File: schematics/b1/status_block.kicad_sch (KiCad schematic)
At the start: 24 parts, among them Q1 2N3904, SW9 SW_SPDT, U3 74HC595

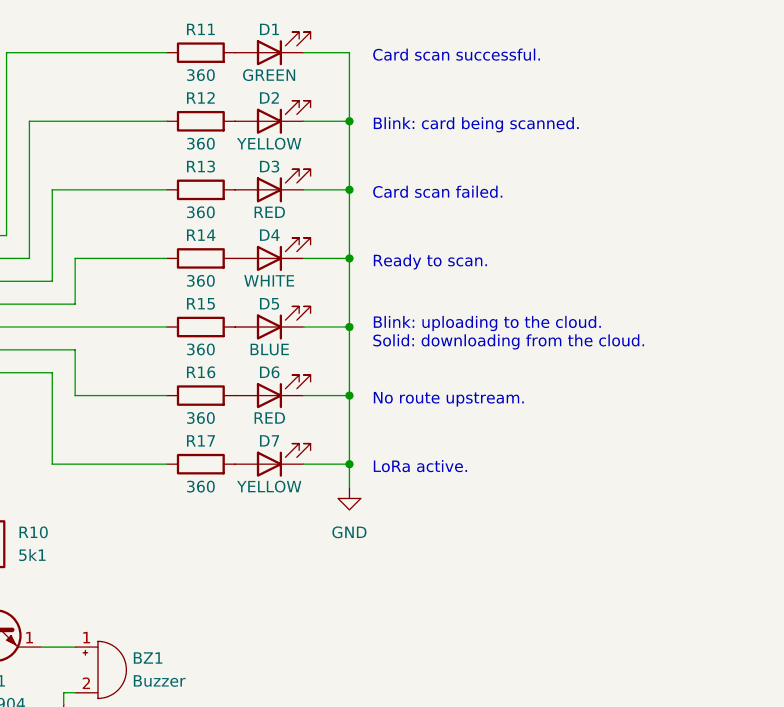
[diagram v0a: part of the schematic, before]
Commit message: Changed status block resistor ordering for simplicity.
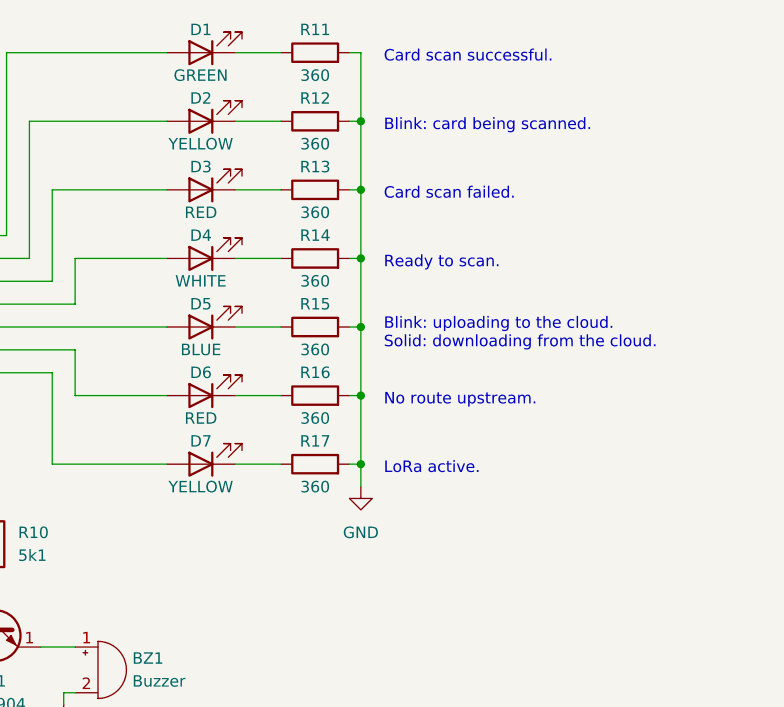
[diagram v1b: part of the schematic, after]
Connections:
- net GND: now also R11.2, R12.2, R13.2, R14.2, R15.2, R16.2, R17.2; no longer D1.1 (K), D2.1 (K), D3.1 (K), D4.1 (K), D5.1 (K), D6.1 (K), D7.1 (K)
- net at D7.2 (A): now also U3.6 (QG); no longer R17.2
- net at D5.2 (A): now also U3.4 (QE); no longer R15.2
- net at U3.3 (QD): now also D4.2 (A); no longer R14.1
- net at R12.1: now also D2.1 (K); no longer U3.1 (QB)
- net at R11.1: now also D1.1 (K); no longer U3.15 (QA)
- net at U3.2 (QC): now also D3.2 (A); no longer R13.1
- net at R15.1: now also D5.1 (K); no longer U3.4 (QE)
- net at U3.5 (QF): now also D6.2 (A); no longer R16.1
- net at R17.1: now also D7.1 (K); no longer U3.6 (QG)
- net at D1.2 (A): now also U3.15 (QA); no longer R11.2
- net at D2.2 (A): now also U3.1 (QB); no longer R12.2
- new net: D6.1 (K), R16.1
- new net: D3.1 (K), R13.1
- new net: D4.1 (K), R14.1
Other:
- moved on the sheet: D1, D2, D3, D4, D5, D6, D7

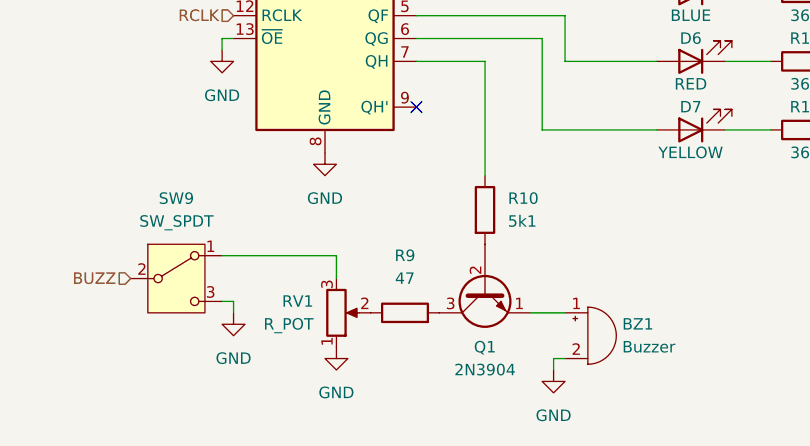
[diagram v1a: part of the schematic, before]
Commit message: Updated the status block.
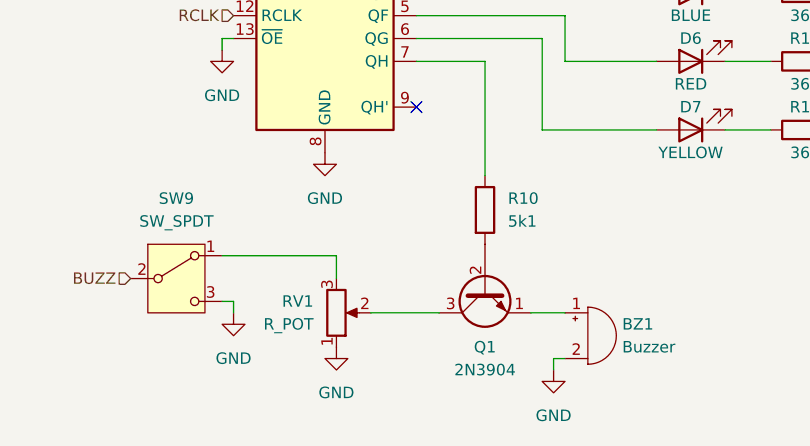
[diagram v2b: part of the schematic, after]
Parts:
- removed R9: 47, symbol Device:R
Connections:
- net at RV1.2: now also Q1.3 (C)
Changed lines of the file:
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@@
+    (stroke (width 0) (type default))
+  )
+  (wire (pts (xy 83.82 87.63) (xy 91.44 87.63))
     (stroke (width 0) (type default))
   )
@@
         )
       )
-    )
-  )
-  (symbol (lib_id "Device:R") (at 87.63 87.63 90) (unit 1)
-    (in_bom yes) (on_board yes) (dnp no) (fields_autoplaced)
-    (property "Reference" "R9" (at 87.63 81.28 90)
-      (effects (font (size 1.27 1.27)))
-    )
-    (property "Value" "47" (at 87.63 83.82 90)
-      (effects (font (size 1.27 1.27)))
-    )
-    (property "Footprint" "" (at 87.63 89.408 90)
-      (effects (font (size 1.27 1.27)) hide)
-    )
-    (property "Datasheet" "~" (at 87.63 87.63 0)
-      (effects (font (size 1.27 1.27)) hide)
-    )
-    (pin "1")
-    (pin "2")
-    (instances
-      (project "b1"
-        (path "/d6142fa5-2354-4512-9919-37616259c364/fdcf7d10-3243-4165-8310-96b25d91ab12"
-          (reference "R9") (unit 1)
-        )
-      )

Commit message: Updated annotations.
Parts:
- renumbered D1 to D2, D2 to D3, D3 to D4, D4 to D5, D5 to D6, D6 to D7, D7 to D8, R10 to R14, R11 to R15, R12 to R16, R13 to R17, R14 to R18, R15 to R19, R16 to R20, R17 to R21, SW9 to SW5, U3 to U4

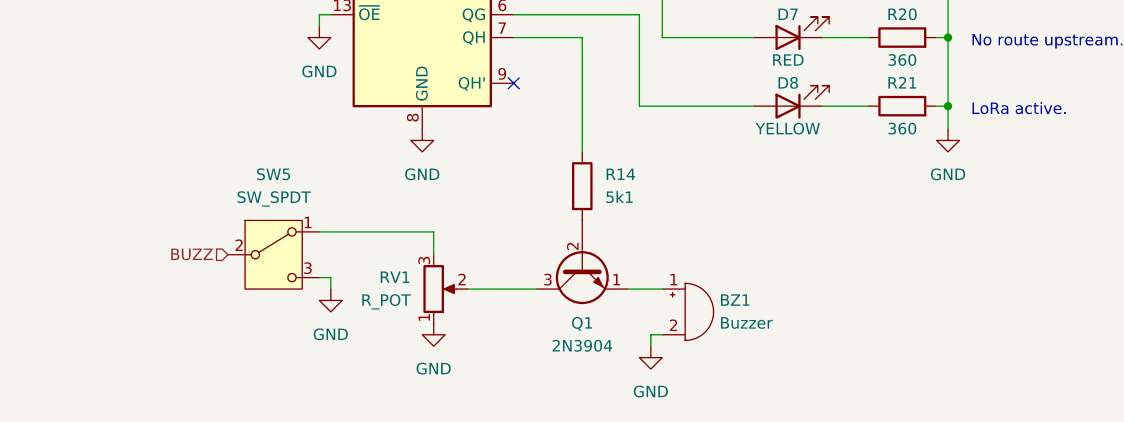
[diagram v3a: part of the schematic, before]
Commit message: Got rid of a potentiometer in favor of a cheaper hardcoded value.
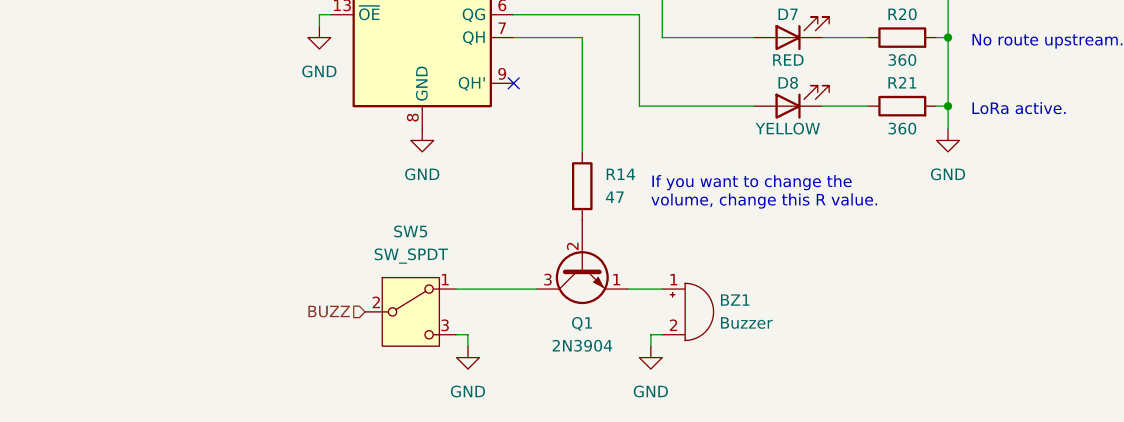
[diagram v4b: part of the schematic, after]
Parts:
- removed RV1: R_POT, symbol Device:R_Potentiometer
- R14: value 5k1 -> 47
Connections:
- net at Q1.3 (C): now also SW5.1 (A)
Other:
- note added: "If you want to change the volume, change this R value."
- moved on the sheet: SW5
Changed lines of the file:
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@@
     (stroke (width 0) (type default))
   )
-  (wire (pts (xy 83.82 87.63) (xy 91.44 87.63))
+  (wire (pts (xy 82.55 87.63) (xy 91.44 87.63))
     (stroke (width 0) (type default))
   )
@@
     (stroke (width 0) (type default))
   )
-  (wire (pts (xy 67.31 81.28) (xy 80.01 81.28))
-    (stroke (width 0) (type default))
-  )
   (wire (pts (xy 104.14 92.71) (xy 104.14 93.98))
     (stroke (width 0) (type default))
@@
     (stroke (width 0) (type default))
   )
-  (wire (pts (xy 67.31 86.36) (xy 68.58 86.36))
+  (wire (pts (xy 82.55 92.71) (xy 83.82 92.71))
     (stroke (width 0) (type default))
   )
@@
     (stroke (width 0) (type default))
   )
-  (wire (pts (xy 80.01 81.28) (xy 80.01 83.82))
-    (stroke (width 0) (type default))
-  )
   (wire (pts (xy 137.16 21.59) (xy 137.16 29.21))
     (stroke (width 0) (type default))
@@
     (stroke (width 0) (type default))
   )
-  (wire (pts (xy 68.58 86.36) (xy 68.58 87.63))
+  (wire (pts (xy 83.82 92.71) (xy 83.82 93.98))
     (stroke (width 0) (type default))
   )
@@
   )
   (text "Blink: card being scanned." (at 139.7 30.48 0)
+    (effects (font (size 1.27 1.27)) (justify left bottom))
+  )
+  (text "If you want to change the\nvolume, change this R value."
+    (at 104.14 78.74 0)
     (effects (font (size 1.27 1.27)) (justify left bottom))
   )
@@
     (effects (font (size 1.27 1.27)) (justify left))
   )
-  (hierarchical_label "BUZZ" (shape input) (at 57.15 83.82 180) (fields_autoplaced)
+  (hierarchical_label "BUZZ" (shape input) (at 72.39 90.17 180) (fields_autoplaced)
     (effects (font (size 1.27 1.27)) (justify right))
   )
@@
     )
   )
-  (symbol (lib_id "power:GND") (at 68.58 87.63 0) (unit 1)
-    (in_bom yes) (on_board yes) (dnp no) (fields_autoplaced)
-    (property "Reference" "#PWR012" (at 68.58 93.98 0)
-      (effects (font (size 1.27 1.27)) hide)
-    )
-    (property "Value" "GND" (at 68.58 92.71 0)
-      (effects (font (size 1.27 1.27)))
-    )
-    (property "Footprint" "" (at 68.58 87.63 0)
-      (effects (font (size 1.27 1.27)) hide)
-    )
-    (property "Datasheet" "" (at 68.58 87.63 0)
+  (symbol (lib_id "power:GND") (at 83.82 93.98 0) (unit 1)
+    (in_bom yes) (on_board yes) (dnp no) (fields_autoplaced)
+    (property "Reference" "#PWR012" (at 83.82 100.33 0)
+      (effects (font (size 1.27 1.27)) hide)
+    )
+    (property "Value" "GND" (at 83.82 99.06 0)
+      (effects (font (size 1.27 1.27)))
+    )
+    (property "Footprint" "" (at 83.82 93.98 0)
+      (effects (font (size 1.27 1.27)) hide)
+    )
+    (property "Datasheet" "" (at 83.82 93.98 0)
       (effects (font (size 1.27 1.27)) hide)
     )
@@
     )
   )
-  (symbol (lib_id "power:GND") (at 80.01 91.44 0) (unit 1)
-    (in_bom yes) (on_board yes) (dnp no) (fields_autoplaced)
-    (property "Reference" "#PWR014" (at 80.01 97.79 0)
-      (effects (font (size 1.27 1.27)) hide)
-    )
-    (property "Value" "GND" (at 80.01 96.52 0)
-      (effects (font (size 1.27 1.27)))
-    )
-    (property "Footprint" "" (at 80.01 91.44 0)
-      (effects (font (size 1.27 1.27)) hide)
-    )
-    (property "Datasheet" "" (at 80.01 91.44 0)
-      (effects (font (size 1.27 1.27)) hide)
-    )
-    (pin "1")
-    (instances
-      (project "b1"
-        (path "/d6142fa5-2354-4512-9919-37616259c364/fdcf7d10-3243-4165-8310-96b25d91ab12"
-          (reference "#PWR014") (unit 1)
-        )
-      )
-    )
-  )
   (symbol (lib_id "Device:LED") (at 119.38 59.69 180) (unit 1)
     (in_bom yes) (on_board yes) (dnp no)
@@
         (path "/d6142fa5-2354-4512-9919-37616259c364/fdcf7d10-3243-4165-8310-96b25d91ab12"
           (reference "C6") (unit 1)
-        )
-      )
-    )
-  )
-  (symbol (lib_id "Device:R_Potentiometer") (at 80.01 87.63 0) (mirror x) (unit 1)
-    (in_bom yes) (on_board yes) (dnp no)
-    (property "Reference" "RV1" (at 77.47 86.36 0)
-      (effects (font (size 1.27 1.27)) (justify right))
-    )
-    (property "Value" "R_POT" (at 77.47 88.9 0)
-      (effects (font (size 1.27 1.27)) (justify right))
-    )
-    (property "Footprint" "" (at 80.01 87.63 0)
-      (effects (font (size 1.27 1.27)) hide)
-    )
-    (property "Datasheet" "~" (at 80.01 87.63 0)
-      (effects (font (size 1.27 1.27)) hide)
-    )
-    (pin "1")
-    (pin "2")
-    (pin "3")
-    (instances
-      (project "b1"
-        (path "/d6142fa5-2354-4512-9919-37616259c364/fdcf7d10-3243-4165-8310-96b25d91ab12"
-          (reference "RV1") (unit 1)
         )
       )
@@
       (effects (font (size 1.27 1.27)) (justify left))
     )
-    (property "Value" "5k1" (at 99.06 77.47 0)
+    (property "Value" "47" (at 99.06 77.47 0)
       (effects (font (size 1.27 1.27)) (justify left))
     )
@@
     )
   )
-  (symbol (lib_id "Switch:SW_SPDT") (at 62.23 83.82 0) (unit 1)
-    (in_bom yes) (on_board yes) (dnp no) (fields_autoplaced)
-    (property "Reference" "SW5" (at 62.23 74.93 0)
-      (effects (font (size 1.27 1.27)))
-    )
-    (property "Value" "SW_SPDT" (at 62.23 77.47 0)
-      (effects (font (size 1.27 1.27)))
-    )
-    (property "Footprint" "" (at 62.23 83.82 0)
-      (effects (font (size 1.27 1.27)) hide)
-    )
-    (property "Datasheet" "~" (at 62.23 91.44 0)
-      (effects (font (size 1.27 1.27)) hide)
-    )
+  (symbol (lib_id "Switch:SW_SPDT") (at 77.47 90.17 0) (unit 1)
+    (in_bom yes) (on_board yes) (dnp no) (fields_autoplaced)
+    (property "Reference" "SW5" (at 77.47 81.28 0)
+      (effects (font (size 1.27 1.27)))
+    )
+    (property "Value" "SW_SPDT" (at 77.47 83.82 0)
+      (effects (font (size 1.27 1.27)))
+    )
+    (property "Footprint" "" (at 77.47 90.17 0)
+      (effects (font (size 1.27 1.27)) hide)
+    )
+    (property "Datasheet" "~" (at 77.47 97.79 0)
+      (effects (font (size 1.27 1.27)) hide)
+    )

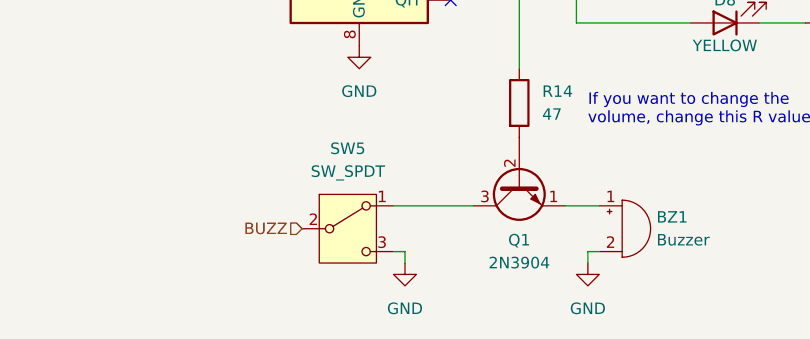
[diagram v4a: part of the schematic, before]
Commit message: Removed bad connection.
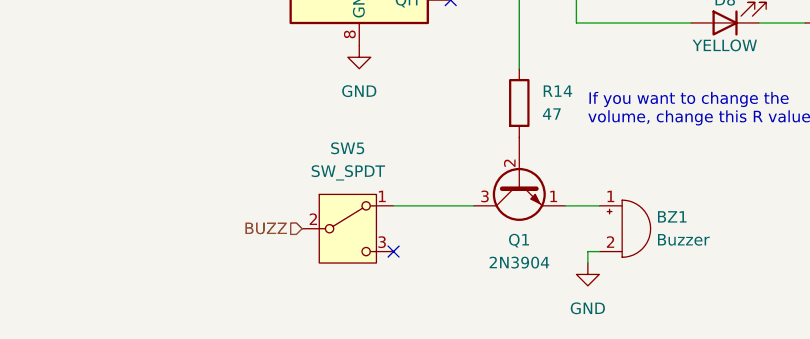
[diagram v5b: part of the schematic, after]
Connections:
- net GND: no longer SW5.3 (C)
- no-connect marks 1 -> 2
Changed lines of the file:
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@@
   (junction (at 137.16 36.83) (diameter 0) (color 0 0 0 0)
   )
+  (no_connect (at 82.55 92.71))
   (no_connect (at 88.9 64.77))
   (wire (pts (xy 78.74 25.4) (xy 59.69 25.4))
@@
     (stroke (width 0) (type default))
   )
-  (wire (pts (xy 82.55 92.71) (xy 83.82 92.71))
-    (stroke (width 0) (type default))
-  )
   (wire (pts (xy 102.87 36.83) (xy 102.87 46.99))
     (stroke (width 0) (type default))
@@
   )
   (wire (pts (xy 102.87 46.99) (xy 88.9 46.99))
-    (stroke (width 0) (type default))
-  )
-  (wire (pts (xy 83.82 92.71) (xy 83.82 93.98))
     (stroke (width 0) (type default))
   )
@@
         )
       )
-    )
-  )
-  (symbol (lib_id "power:GND") (at 83.82 93.98 0) (unit 1)
-    (in_bom yes) (on_board yes) (dnp no) (fields_autoplaced)
-    (property "Reference" "#PWR012" (at 83.82 100.33 0)
-      (effects (font (size 1.27 1.27)) hide)
-    )
-    (property "Value" "GND" (at 83.82 99.06 0)
-      (effects (font (size 1.27 1.27)))
-    )
-    (property "Footprint" "" (at 83.82 93.98 0)
-      (effects (font (size 1.27 1.27)) hide)
-    )
-    (property "Datasheet" "" (at 83.82 93.98 0)
-      (effects (font (size 1.27 1.27)) hide)
-    )
-    (pin "1")
-    (instances
-      (project "b1"
-        (path "/d6142fa5-2354-4512-9919-37616259c364/fdcf7d10-3243-4165-8310-96b25d91ab12"
-          (reference "#PWR012") (unit 1)
-        )
-      )

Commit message: Updated buzz switch.
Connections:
- net BUZZ: now also Q1.3 (C); no longer SW5.2 (B)
- net GND: now also SW5.3 (C)
- net at Q1.2 (B): now also SW5.1 (A); no longer R14.2
- new net: R14.2, SW5.2 (B)
- no-connect marks 2 -> 1
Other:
- note removed: "If you want to change the volume, change this R value."
- moved on the sheet: BZ1, C4, C5, C6, D2, D3, D4, D5, D6, D7, D8, Q1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

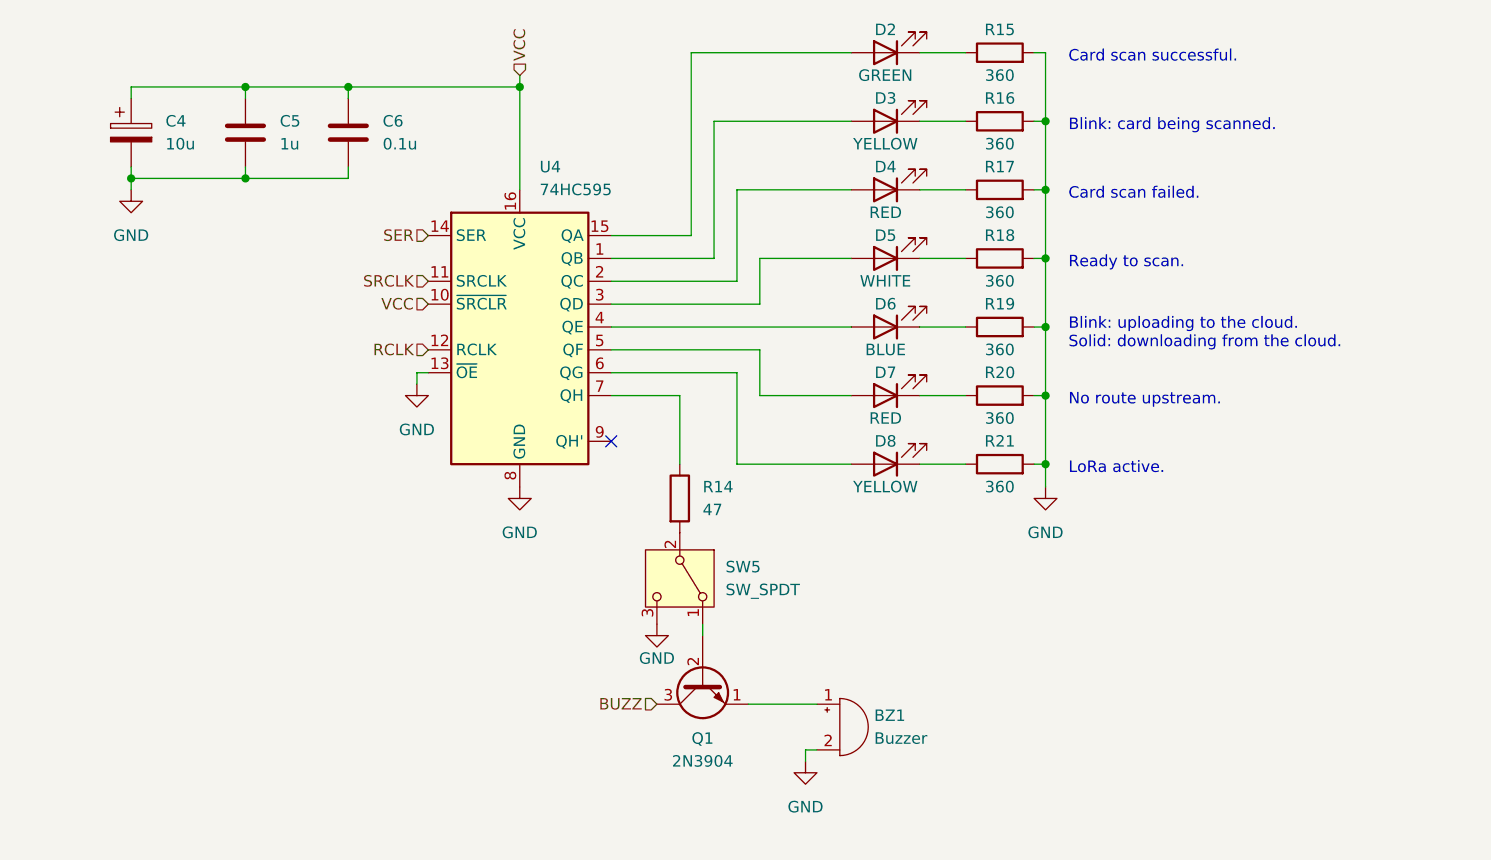
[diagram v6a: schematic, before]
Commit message: Updated status block schematic.
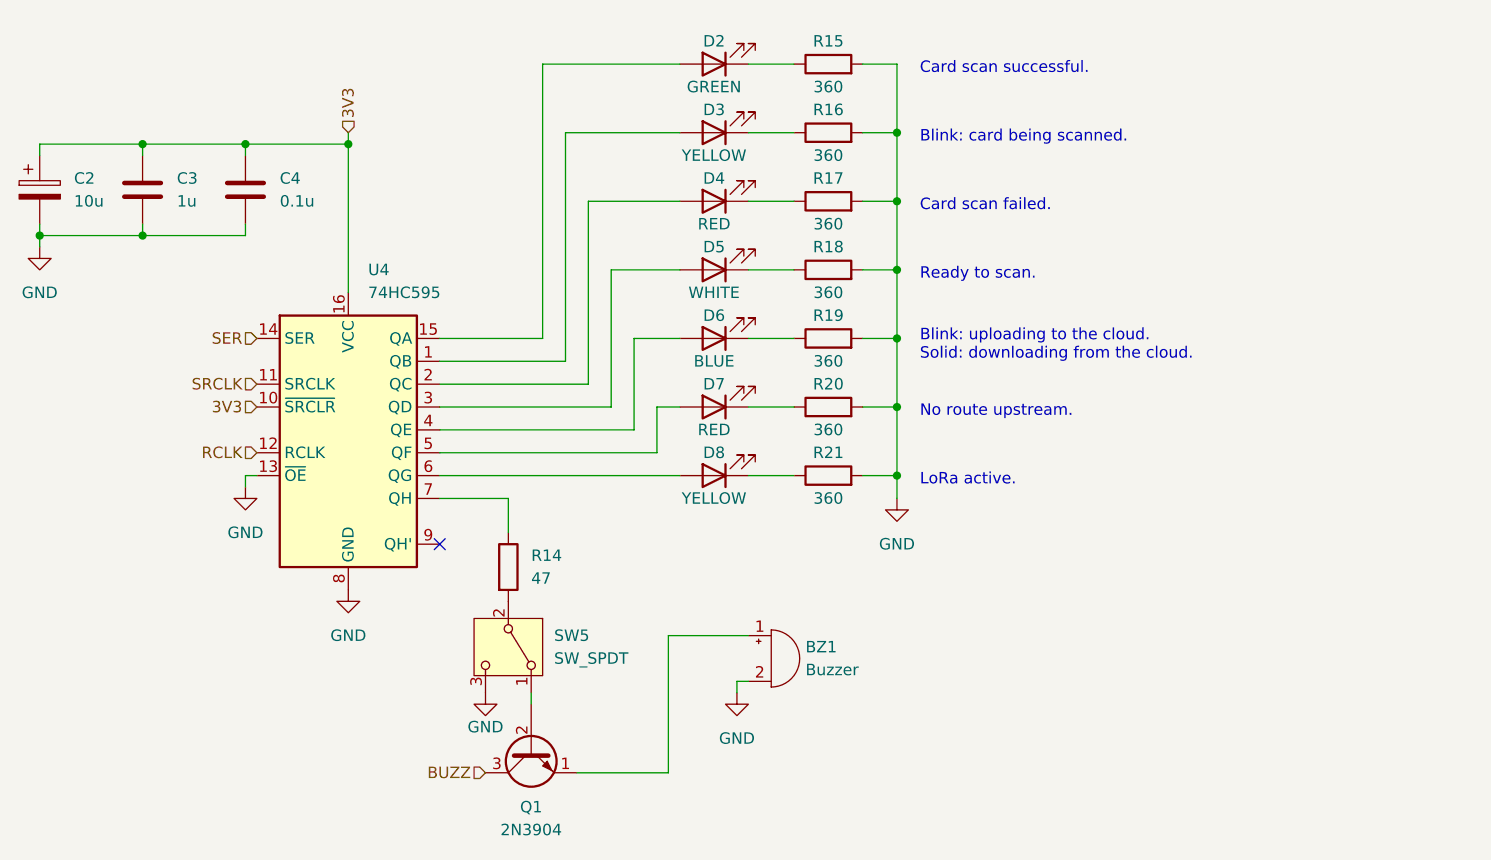
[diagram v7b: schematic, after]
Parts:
- removed C4: 10u, symbol Device:C_Polarized
- removed C5: 1u, symbol Device:C
- removed C6: 0.1u, symbol Device:C
- added C2: 10u, symbol Device:C_Polarized
- added C3: 1u, symbol Device:C
- added C4: 0.1u, symbol Device:C
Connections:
- net GND: now also C2.2, C3.2, C4.2
- net VCC renamed 3V3
- net 3V3: now also C2.1, C3.1, C4.1
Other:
- moved on the sheet: BZ1, D2, D3, D4, D5, D6, D7, D8, Q1, R14, R15, R16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
